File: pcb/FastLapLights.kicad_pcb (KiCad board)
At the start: 4 copper layers, 27.3 x 40 mm, 17 parts, among them J1 POWER_CON, J2 SWD, J3 PWR, J4 I2C, J5 Conn_02x04_Counter_Clockwise, U1 BD33FC0FP, U2 STM32C011F4Px

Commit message: update footprint
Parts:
- C3: value 200uF -> 220uF
- C4, C5: footprint Capacitor_SMD:C_0603_1608Metric -> Capacitor_SMD:C_0805_2012Metric
- moved C4 0.50 mm to (52.9, 107.5)
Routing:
- net /VRAIL_CAP: track 25.3 -> 26.0 mm
- net GND: vias 86 -> 85

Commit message: prep firmware
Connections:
- U2 pad 12: /IO_POWER_RAIL_DATA -> unconnected-(U2-PA5-Pad12)
- U2 pad 13: unconnected-(U2-PA6-Pad13) -> /IO_POWER_RAIL_DATA
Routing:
- net /IO_POWER_RAIL_DATA: track 23.1 -> 23.8 mm
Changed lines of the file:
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@@
 	(net 13 "unconnected-(U2-PA9{slash}PA11-Pad16)")
 	(net 14 "unconnected-(U2-PC15-Pad3)")
-	(net 15 "unconnected-(U2-PA6-Pad13)")
+	(net 15 "unconnected-(U2-PA5-Pad12)")
 	(net 16 "unconnected-(U2-PA10{slash}PA12-Pad17)")
 	(net 17 "VRAIL")
@@
 			(layers "F.Cu" "F.Paste" "F.Mask")
 			(roundrect_rratio 0.25)
-			(net 18 "/IO_POWER_RAIL_DATA")
+			(net 15 "unconnected-(U2-PA5-Pad12)")
 			(pinfunction "PA5")
-			(pintype "bidirectional")
+			(pintype "bidirectional+no_connect")
 		)
 		(pad "13" smd roundrect
@@
 			(layers "F.Cu" "F.Paste" "F.Mask")
 			(roundrect_rratio 0.25)
-			(net 15 "unconnected-(U2-PA6-Pad13)")
+			(net 18 "/IO_POWER_RAIL_DATA")
 			(pinfunction "PA6")
-			(pintype "bidirectional+no_connect")
+			(pintype "bidirectional")
 		)
 		(pad "14" smd roundrect
@@
 		(layer "Cmts.User")
 		(pts
-			(xy 42.5 86.7) (xy 42.5 126.7)
+			(xy 42.5 86.7) (xy 42.5 103.6)
 		)
-		(height 7.799999)
-		(gr_text "40.0000 mm"
-			(at 32.900001 106.7 90)
+		(height 1.6)
+		(gr_text "16.9000 mm"
+			(at 39.75 95.15 90)
 			(layer "Cmts.User")
 			(effects
 				(font
-					(size 1.5 1.5)
-					(thickness 0.3)
+					(size 1 1)
+					(thickness 0.15)
 				)
 			)
@@
 		)
 		(style
-			(thickness 0.2)
+			(thickness 0.1)
 			(arrow_length 1.27)
 			(text_position_mode 0)
@@
 			(xy 42.5 126.7) (xy 69.8 126.7)
 		)
-		(height 8)
+		(height 10.7)
 		(gr_text "27.3000 mm"
-			(at 56.15 132.9 0)
+			(at 56.15 136.25 0)
+			(layer "Cmts.User")
+			(effects
+				(font
+					(size 1 1)
+					(thickness 0.15)
+				)
+			)
+		)
+		(format
+			(prefix "")
+			(suffix "")
+			(units 3)
+			(units_format 1)
+			(precision 4)
+		)
+		(style
+			(thickness 0.1)
+			(arrow_length 1.27)
+			(text_position_mode 0)
+			(extension_height 0.58642)
+			(extension_offset 0.5) keep_text_aligned)
+	)
+	(dimension
+		(type aligned)
+		(layer "Cmts.User")
+		(pts
+			(xy 42.5 86.7) (xy 42.5 114.9)
+		)
+		(height 6.9)
+		(gr_text "28.2000 mm"
+			(at 34.45 100.8 90)
 			(layer "Cmts.User")
 			(effects
 				(font
-					(size 1.5 1.5)
-					(thickness 0.3)
+					(size 1 1)
+					(thickness 0.15)
 				)
 			)
@@
 		)
 		(style
-			(thickness 0.2)
+			(thickness 0.1)
+			(arrow_length 1.27)
+			(text_position_mode 0)
+			(extension_height 0.58642)
+			(extension_offset 0.5) keep_text_aligned)
+	)
+	(dimension
+		(type aligned)
+		(layer "Cmts.User")
+		(pts
+			(xy 42.5 86.7) (xy 42.5 109.9)
+		)
+		(height 4.2)
+		(gr_text "23.2000 mm"
+			(at 37.15 98.3 90)
+			(layer "Cmts.User")
+			(effects
+				(font
+					(size 1 1)
+					(thickness 0.15)
+				)
+			)
+		)
+		(format
+			(prefix "")
+			(suffix "")
+			(units 3)
+			(units_format 1)
+			(precision 4)
+		)
+		(style
+			(thickness 0.1)
+			(arrow_length 1.27)
+			(text_position_mode 0)
+			(extension_height 0.58642)
+			(extension_offset 0.5) keep_text_aligned)
+	)
+	(dimension
+		(type aligned)
+		(layer "Cmts.User")
+		(pts
+			(xy 49.25 114.9) (xy 42.5 114.9)
+		)
+		(height -14.9)
+		(gr_text "6.75 mm"
+			(at 45.875 128.65 0)
+			(layer "Cmts.User")
+			(effects
+				(font
+					(size 1 1)
+					(thickness 0.15)
+				)
+			)
+		)
+		(format
+			(prefix "")
+			(suffix "")
+			(units 3)
+			(units_format 1)
+			(precision 2)
+		)
+		(style
+			(thickness 0.1)
+			(arrow_length 1.27)
+			(text_position_mode 0)
+			(extension_height 0.58642)
+			(extension_offset 0.5) keep_text_aligned)
+	)
+	(dimension
+		(type aligned)
+		(layer "Cmts.User")
+		(pts
+			(xy 55.4 114.9) (xy 42.5 114.9)
+		)
+		(height -17.8)
+		(gr_text "12.9000 mm"
+			(at 48.95 131.55 0)
+			(layer "Cmts.User")
+			(effects
+				(font
+					(size 1 1)
+					(thickness 0.15)
+				)
+			)
+		)
+		(format
+			(prefix "")
+			(suffix "")
+			(units 3)
+			(units_format 1)
+			(precision 4)
+		)
+		(style
+			(thickness 0.1)
+			(arrow_length 1.27)
+			(text_position_mode 0)
+			(extension_height 0.58642)
+			(extension_offset 0.5) keep_text_aligned)
+	)
+	(dimension
+		(type aligned)
+		(layer "Cmts.User")
+		(pts
+			(xy 42.5 86.7) (xy 42.5 126.7)
+		)
+		(height 9.9)
+		(gr_text "40.0000 mm"
+			(at 31.45 106.7 90)
+			(layer "Cmts.User")
+			(effects
+				(font
+					(size 1 1)
+					(thickness 0.15)
+				)
+			)
+		)
+		(format
+			(prefix "")
+			(suffix "")
+			(units 3)
+			(units_format 1)
+			(precision 4)
+		)
+		(style
+			(thickness 0.1)
 			(arrow_length 1.27)
 			(text_position_mode 0)
@@
 	)
 	(segment
+		(start 56.4 119.275)
+		(end 56.4 118.2)
+		(width 0.4)
+		(layer "F.Cu")
+		(net 3)
+	)
+	(segment
+		(start 56.4 117.9)
+		(end 56.425 117.875)
+		(width 0.7)
+		(layer "F.Cu")
+		(net 3)
+	)
+	(segment
 		(start 58.225 103.0275)
 		(end 58.2525 103)
@@
 	)
 	(segment
-		(start 56.4 118.1)
-		(end 56.425 118.075)
-		(width 0.4)
-		(layer "F.Cu")
-		(net 3)
-	)
-	(segment
 		(start 55.225 105.125)
 		(end 56.4 105.125)
@@
 	)
 	(segment
+		(start 56.425 117.875)
+		(end 56.425 117.3)
+		(width 0.7)
+		(layer "F.Cu")
+		(net 3)
+	)
+	(segment
 		(start 57.05 115.6)
 		(end 57.05 114.55)
@@
 	)
 	(segment
-		(start 56.4 119.275)
-		(end 56.4 118.1)
-		(width 0.4)
-		(layer "F.Cu")
-		(net 3)
-	)
-	(segment
 		(start 56.4 103.5)
 		(end 56.4 105.125)
@@
 	)
 	(segment
-		(start 57.05 115.6)
-		(end 57.05 116.05)
-		(width 0.8)
+		(start 56.4 118.2)
+		(end 56.4 117.9)
+		(width 0.7)
 		(layer "F.Cu")
 		(net 3)
 	)
 	(segment
-		(start 56.425 118.075)
-		(end 56.425 117.3)
-		(width 0.4)
+		(start 57.05 115.6)
+		(end 57.05 116.05)
+		(width 0.8)
 		(layer "F.Cu")
 		(net 3)
@@
 	)
 	(segment
-		(start 51.4 121.9)
-		(end 47.6 121.9)
+		(start 52.2 121.9)
+		(end 53.8 123.5)
 		(width 0.4)
 		(layer "F.Cu")
@@
 	)
 	(segment
-		(start 53.15 123.65)
-		(end 51.4 121.9)
+		(start 47.6 121.9)
+		(end 52.2 121.9)
 		(width 0.4)
 		(layer "F.Cu")
@@
 	)
 	(segment
-		(start 47.6 121.9)
-		(end 47.4 121.7)
+		(start 47.4 121.7)
+		(end 47.6 121.9)
 		(width 0.4)
 		(layer "F.Cu")
@@
 	)
 	(segment
-		(start 53.15 125)
-		(end 53.15 123.65)
+		(start 53.8 123.5)
+		(end 53.8 125)
 		(width 0.4)
 		(layer "F.Cu")

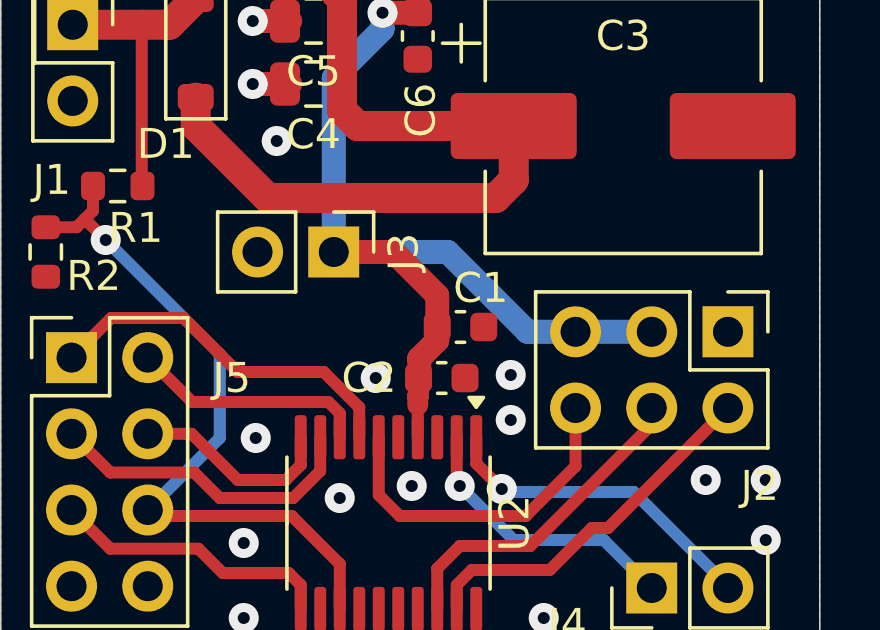
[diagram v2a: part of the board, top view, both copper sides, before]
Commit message: migrate ws2812b and manchester decoder
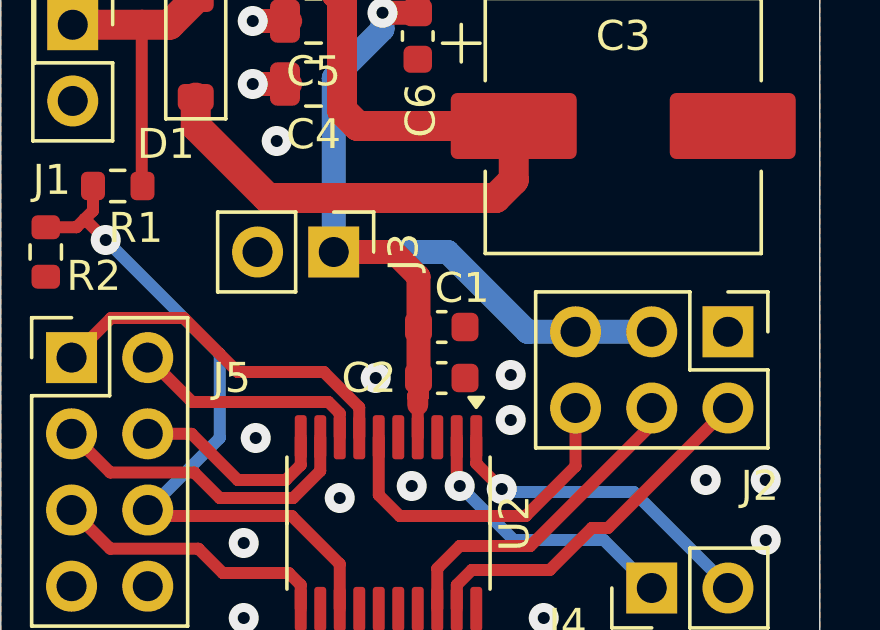
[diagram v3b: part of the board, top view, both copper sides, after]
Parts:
- moved C1 0.62 mm to (57.2, 115.6)
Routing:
- net +3.3V: track 34.3 -> 33.8 mm
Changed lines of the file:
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@@
 	(footprint "Capacitor_SMD:C_0603_1608Metric"
 		(layer "F.Cu")
-		(at 57.825 115.6)
+		(at 57.2 115.6)
 		(descr "Capacitor SMD 0603 (1608 Metric), square (rectangular) end terminal, IPC_7351 nominal, (Body size source: IPC-SM-782 page 76, https://www.pcb-3d.com/wordpress/wp-content/uploads/ipc-sm-782a_amendment_1_and_2.pdf), generated with kicad-footprint-generator")
 		(tags "capacitor")
@@
 	)
 	(segment
+		(start 56.425 115.6)
+		(end 56.425 113.925)
+		(width 0.8)
+		(layer "F.Cu")
+		(net 3)
+	)
+	(segment
 		(start 58.225 103.0275)
 		(end 58.2525 103)
@@
 	)
 	(segment
+		(start 56.425 115.6)
+		(end 56.425 117.3)
+		(width 0.8)
+		(layer "F.Cu")
+		(net 3)
+	)
+	(segment
 		(start 55.6 113.1)
 		(end 53.6 113.1)
@@
 	)
 	(segment
+		(start 56.425 113.925)
+		(end 55.6 113.1)
+		(width 0.8)
+		(layer "F.Cu")
+		(net 3)
+	)
+	(segment
 		(start 56.425 117.875)
 		(end 56.425 117.3)
@@
 	)
 	(segment
-		(start 57.05 115.6)
-		(end 57.05 114.55)
-		(width 0.8)
-		(layer "F.Cu")
-		(net 3)
-	)
-	(segment
-		(start 57.05 114.55)
-		(end 55.6 113.1)
-		(width 0.8)
-		(layer "F.Cu")
-		(net 3)
-	)
-	(segment
-		(start 57.05 116.05)
-		(end 56.45 116.65)
-		(width 0.8)
-		(layer "F.Cu")
-		(net 3)
-	)
-	(segment
 		(start 56.4 103.5)
 		(end 56.4 105.125)
@@
 	)
 	(segment
-		(start 56.45 116.65)
-		(end 56.45 117.3)
-		(width 0.8)
-		(layer "F.Cu")
-		(net 3)
-	)
-	(segment
 		(start 56.4 118.2)
 		(end 56.4 117.9)
@@
 		(layer "F.Cu")
 		(net 3)
-	)
-	(segment
-		(start 57.05 115.6)
-		(end 57.05 116.05)
-		(width 0.8)
-		(layer "F.Cu")
-		(net 3)

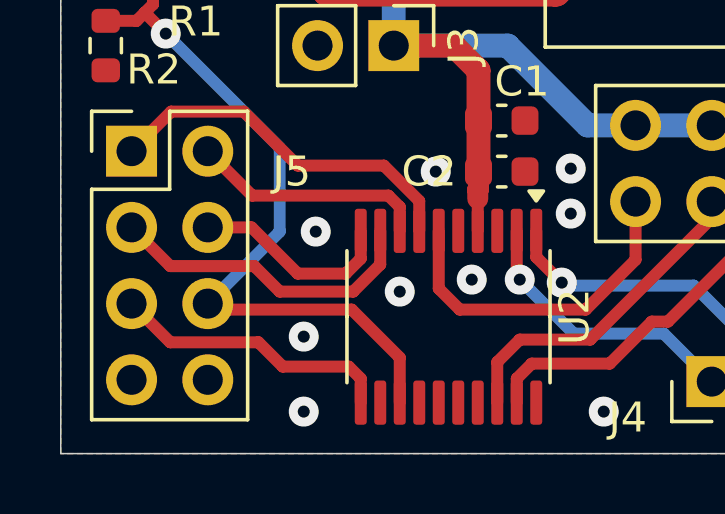
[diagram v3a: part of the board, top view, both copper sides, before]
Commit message: migrate track lights
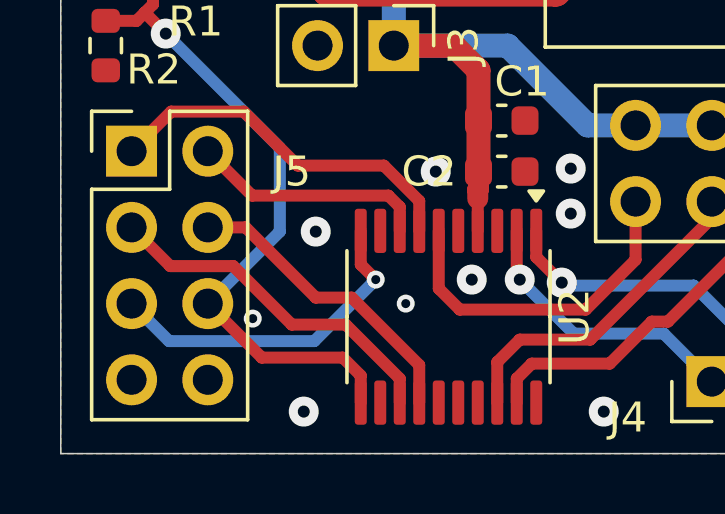
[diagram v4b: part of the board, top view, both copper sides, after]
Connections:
- J5 pad 3: /TRACK_LIGHTS_R -> /TRACK_LIGHTS_G
- J5 pad 4: /TRACK_LIGHTS_G -> /TRACK_LIGHTS_R
- J5 pad 5: /IO_DATA_INT -> /IO_POWER_RAIL_INT
- U2 pad 10: /TRACK_LIGHTS_G -> /IO_POWER_RAIL_INT
- U2 pad 11: /IO_DATA_INT -> /IO_POWER_RAIL_DATA
- U2 pad 13: /IO_POWER_RAIL_DATA -> /TRACK_LIGHTS_G
- U2 pad 14: unconnected-(U2-PA7-Pad14) -> /TRACK_LIGHTS_R
- U2 pad 9: /TRACK_LIGHTS_R -> unconnected-(U2-PA2-Pad9)
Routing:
- net /IO_POWER_RAIL_INT: track 0.00 -> 11.3 mm, vias 0 -> 1
- net /IO_DATA_INT: track 9.48 -> 0.00 mm
- net /TRACK_LIGHTS_G: track 6.87 -> 11.8 mm
- net /IO_POWER_RAIL_DATA: track 23.8 -> 22.2 mm
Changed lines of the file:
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@@
 	(net 5 "/PIT_LANE_LIGHTS")
 	(net 6 "unconnected-(U2-PA8-Pad15)")
-	(net 7 "unconnected-(U2-PA7-Pad14)")
+	(net 7 "unconnected-(U2-PA2-Pad9)")
 	(net 8 "/SWD_NRST")
 	(net 9 "/SWD_SWCLK")
@@
 	(net 19 "/VRAIL_CAP")
 	(net 20 "/TRACK_LIGHTS_G")
-	(net 21 "/IO_DATA_INT")
-	(net 22 "unconnected-(U2-PB6-Pad20)")
+	(net 21 "unconnected-(U2-PB6-Pad20)")
+	(net 22 "/IO_POWER_RAIL_INT")
 	(footprint "Connector_PinHeader_2.54mm:PinHeader_2x04_P2.54mm_Vertical"
 		(layer "F.Cu")
@@
 			)
 			(remove_unused_layers no)
-			(net 2 "/TRACK_LIGHTS_R")
+			(net 20 "/TRACK_LIGHTS_G")
 			(pinfunction "Pin_3")
 			(pintype "passive")
@@
 			)
 			(remove_unused_layers no)
-			(net 20 "/TRACK_LIGHTS_G")
+			(net 2 "/TRACK_LIGHTS_R")
 			(pinfunction "Pin_4")
 			(pintype "passive")
@@
 			)
 			(remove_unused_layers no)
-			(net 21 "/IO_DATA_INT")
+			(net 22 "/IO_POWER_RAIL_INT")
 			(pinfunction "Pin_5")
 			(pintype "passive")
@@
 			(layers "F.Cu" "F.Paste" "F.Mask")
 			(roundrect_rratio 0.25)
-			(net 2 "/TRACK_LIGHTS_R")
+			(net 7 "unconnected-(U2-PA2-Pad9)")
 			(pinfunction "PA2")
-			(pintype "bidirectional")
+			(pintype "bidirectional+no_connect")
 		)
 		(pad "10" smd roundrect
@@
 			(layers "F.Cu" "F.Paste" "F.Mask")
 			(roundrect_rratio 0.25)
-			(net 20 "/TRACK_LIGHTS_G")
+			(net 22 "/IO_POWER_RAIL_INT")
 			(pinfunction "PA3")
 			(pintype "bidirectional")
@@
 			(layers "F.Cu" "F.Paste" "F.Mask")
 			(roundrect_rratio 0.25)
-			(net 21 "/IO_DATA_INT")
+			(net 18 "/IO_POWER_RAIL_DATA")
 			(pinfunction "PA4")
 			(pintype "bidirectional")
@@
 			(layers "F.Cu" "F.Paste" "F.Mask")
 			(roundrect_rratio 0.25)
-			(net 18 "/IO_POWER_RAIL_DATA")
+			(net 20 "/TRACK_LIGHTS_G")
 			(pinfunction "PA6")
 			(pintype "bidirectional")
@@
 			(layers "F.Cu" "F.Paste" "F.Mask")
 			(roundrect_rratio 0.25)
-			(net 7 "unconnected-(U2-PA7-Pad14)")
+			(net 2 "/TRACK_LIGHTS_R")
 			(pinfunction "PA7")
-			(pintype "bidirectional+no_connect")
+			(pintype "bidirectional")
 		)
 		(pad "15" smd roundrect
@@
 			(layers "F.Cu" "F.Paste" "F.Mask")
 			(roundrect_rratio 0.25)
-			(net 22 "unconnected-(U2-PB6-Pad20)")
+			(net 21 "unconnected-(U2-PB6-Pad20)")
 			(pinfunction "PB6")
 			(pintype "bidirectional+no_connect")
@@
 	)
 	(via
+		(at 54 121.7)
+		(size 0.6)
+		(drill 0.3)
+		(layers "F.Cu" "B.Cu")
+		(free yes)
+		(net 1)
+	)
+	(via
 		(at 57 87.7)
 		(size 1)
@@
 	)
 	(via
-		(at 50.6 122.8)
-		(size 1)
-		(drill 0.4)
-		(layers "F.Cu" "B.Cu")
-		(free yes)
-		(net 1)
-	)
-	(via
 		(at 47 97.7)
 		(size 1)
@@
 	)
 	(via
-		(at 53.8 121.3)
-		(size 1)
-		(drill 0.4)
-		(layers "F.Cu" "B.Cu")
-		(free yes)
-		(net 1)
-	)
-	(via
 		(at 65 91.7)
 		(size 1)
@@
 	)
 	(via
+		(at 48.9 122.2)
+		(size 0.6)
+		(drill 0.3)
+		(layers "F.Cu" "B.Cu")
+		(free yes)
+		(net 1)
+	)
+	(via
 		(at 59.5 118.7)
 		(size 1)
@@
 	)
 	(segment
-		(start 52.248528 121.3)
-		(end 49.8 121.3)
-		(width 0.4)
-		(layer "F.Cu")
-		(net 2)
-	)
-	(segment
-		(start 53.15 119.275)
-		(end 53.15 120.398528)
+		(start 48.66 119.16)
+		(end 47.4 119.16)
 		(width 0.4)
 		(layer "F.Cu")
@@
 	)
 	(segment
-		(start 46.15 120.45)
-		(end 44.86 119.16)
+		(start 52.2 121.5)
+		(end 51 121.5)
 		(width 0.4)
 		(layer "F.Cu")
@@
 	)
 	(segment
-		(start 49.8 121.3)
-		(end 48.95 120.45)
+		(start 54.45 123.75)
+		(end 52.2 121.5)
 		(width 0.4)
 		(layer "F.Cu")
@@
 	)
 	(segment
-		(start 53.15 120.398528)
-		(end 52.248528 121.3)
+		(start 51 121.5)
+		(end 48.66 119.16)
 		(width 0.4)
 		(layer "F.Cu")
@@
 	)
 	(segment
-		(start 48.95 120.45)
-		(end 46.15 120.45)
+		(start 54.45 125)
+		(end 54.45 123.75)
 		(width 0.4)
 		(layer "F.Cu")
@@
 	)
 	(segment
+		(start 52.5 125)
+		(end 52.5 124.1)
+		(width 0.4)
+		(layer "F.Cu")
+		(net 18)
+	)
+	(segment
 		(start 45.3 112)
 		(end 46 112.7)
@@
 	)
 	(segment
-		(start 52.2 121.9)
-		(end 53.8 123.5)
+		(start 49.2 123.5)
+		(end 47.4 121.7)
 		(width 0.4)
 		(layer "F.Cu")
@@
 	)
 	(segment
-		(start 47.6 121.9)
-		(end 52.2 121.9)
+		(start 51.9 123.5)
+		(end 49.2 123.5)
 		(width 0.4)
 		(layer "F.Cu")
@@
 	)
 	(segment
-		(start 47.4 121.7)
-		(end 47.6 121.9)
+		(start 52.5 124.1)
+		(end 51.9 123.5)
 		(width 0.4)
 		(layer "F.Cu")
@@
 	)
 	(segment
-		(start 53.8 123.5)
-		(end 53.8 125)
-		(width 0.4)
-		(layer "F.Cu")
-		(net 18)
-	)
-	(segment
 		(start 45.575 110.9)
 		(end 45.575 111.725)
@@
 	)
 	(segment
-		(start 47.4 119.16)
-		(end 48.86 119.16)
+		(start 53.8 124.202622)
+		(end 51.997378 122.4)
 		(width 0.4)
 		(layer "F.Cu")
@@
 	)
 	(segment
-		(start 50.4 120.7)
-		(end 52 120.7)
+		(start 48.25 120.45)
+		(end 46.15 120.45)
 		(width 0.4)
 		(layer "F.Cu")
@@
 	)
 	(segment
-		(start 52.5 120.2)
-		(end 52.5 119.275)
+		(start 50.2 122.4)
+		(end 48.25 120.45)
 		(width 0.4)
 		(layer "F.Cu")
@@
 	)
 	(segment
-		(start 52 120.7)
-		(end 52.5 120.2)
+		(start 51.997378 122.4)
+		(end 50.2 122.4)
 		(width 0.4)
 		(layer "F.Cu")
@@
 	)
 	(segment
-		(start 48.86 119.16)
-		(end 50.4 120.7)
+		(start 53.8 125)
+		(end 53.8 124.202622)
 		(width 0.4)
 		(layer "F.Cu")
@@
 	)
 	(segment
-		(start 49.09 122.99)
-		(end 46.15 122.99)
+		(start 46.15 120.45)
+		(end 44.86 119.16)
 		(width 0.4)
 		(layer "F.Cu")
-		(net 21)
+		(net 20)
 	)
 	(segment
-		(start 49.9 123.8)
-		(end 49.09 122.99)
+		(start 52.5 120.4)
+		(end 53 120.9)
 		(width 0.4)
 		(layer "F.Cu")
-		(net 21)
+		(net 22)
 	)
 	(segment
-		(start 46.15 122.99)
-		(end 44.86 121.7)
+		(start 52.5 119.275)
+		(end 52.5 120.4)
 		(width 0.4)
 		(layer "F.Cu")
-		(net 21)
+		(net 22)
+	)
+	(via
+		(at 53 120.9)
+		(size 0.6)
+		(drill 0.3)
+		(layers "F.Cu" "B.Cu")
+		(net 22)
 	)
 	(segment
-		(start 52.5 125)
-		(end 52.5 124.2)
+		(start 50.95 122.95)
+		(end 46.11 122.95)
 		(width 0.4)
-		(layer "F.Cu")
-		(net 21)
+		(layer "B.Cu")
+		(net 22)
 	)
 	(segment
-		(start 52.1 123.8)
-		(end 49.9 123.8)
+		(start 46.11 122.95)
+		(end 44.86 121.7)
 		(width 0.4)
-		(layer "F.Cu")
-		(net 21)
+		(layer "B.Cu")
+		(net 22)
 	)
 	(segment
-		(start 52.5 124.2)
-		(end 52.1 123.8)
+		(start 53 120.9)
+		(end 50.95 122.95)
 		(width 0.4)
-		(layer "F.Cu")
-		(net 21)
+		(layer "B.Cu")
+		(net 22)
 	)
 	(zone
